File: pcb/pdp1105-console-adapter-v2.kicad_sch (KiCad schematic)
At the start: 15 parts, among them J1 SCL Connector, J2 Aux Terminal Connector, Q1 MMBT3904, U1 Pico, U2 MAX3232

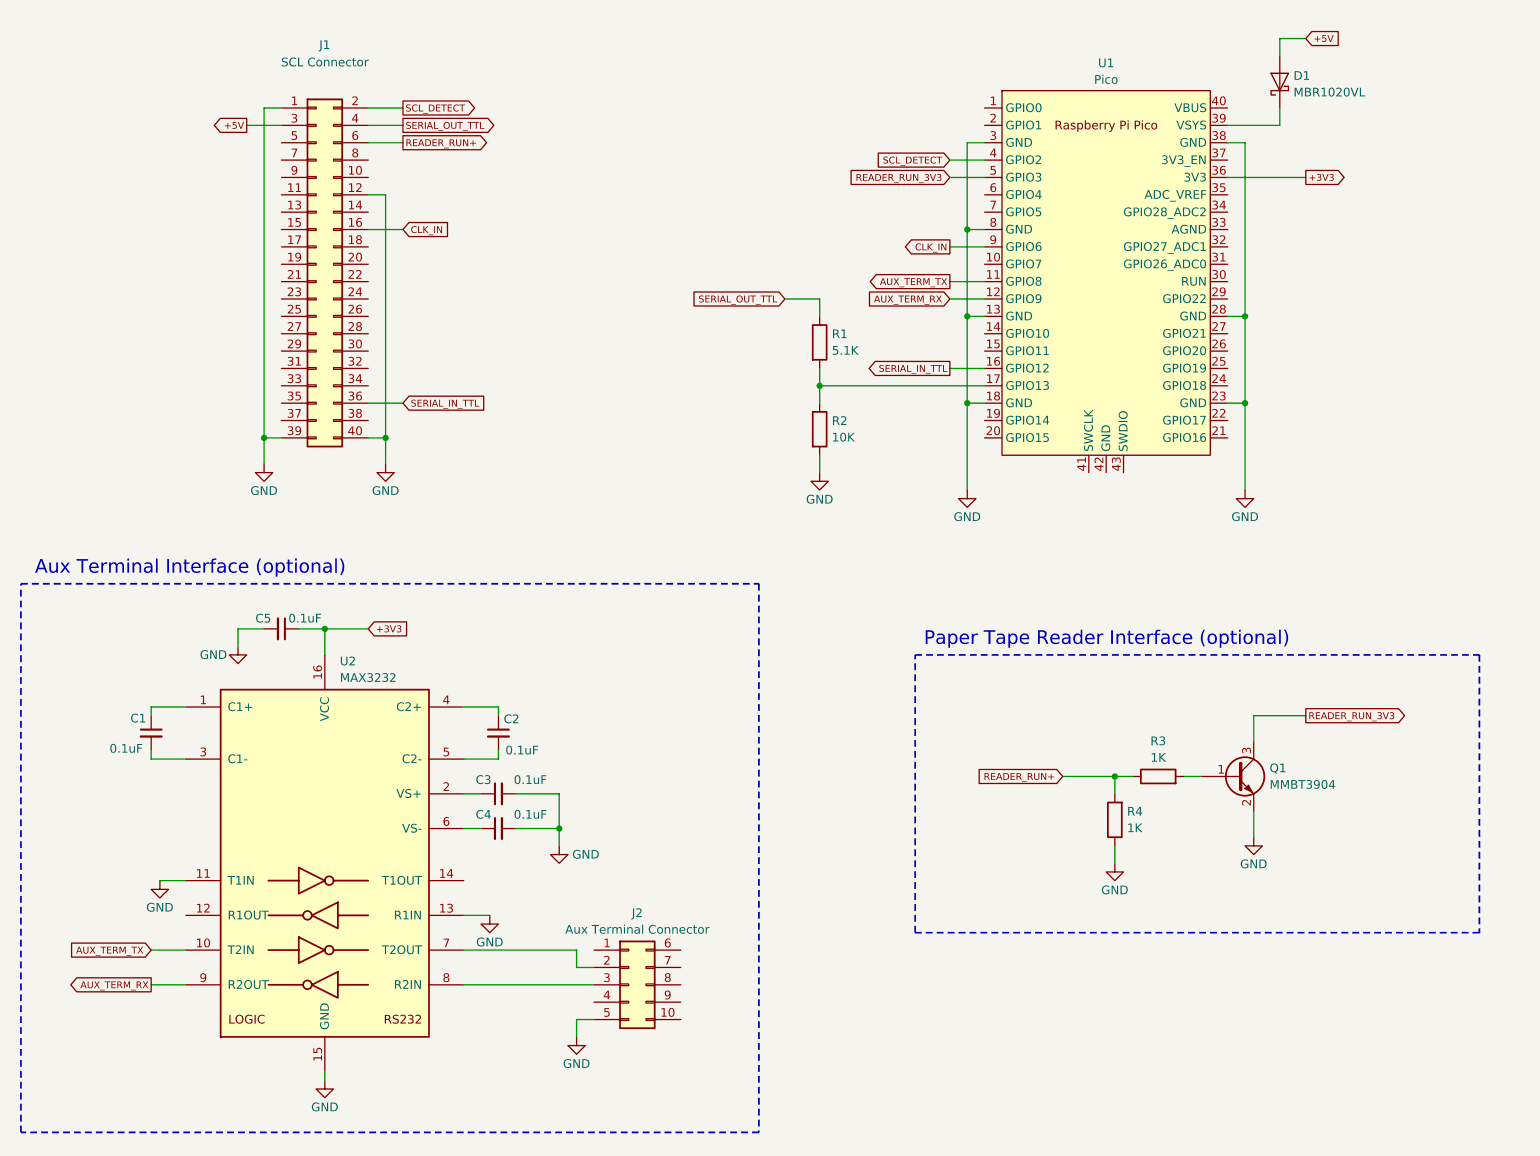
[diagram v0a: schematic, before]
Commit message: ﻿Initial version of Rev 4 schematic
-- Added status LEDs

-- Changed Aux port connector to board-mounted DE9

-- Added mounting hole components
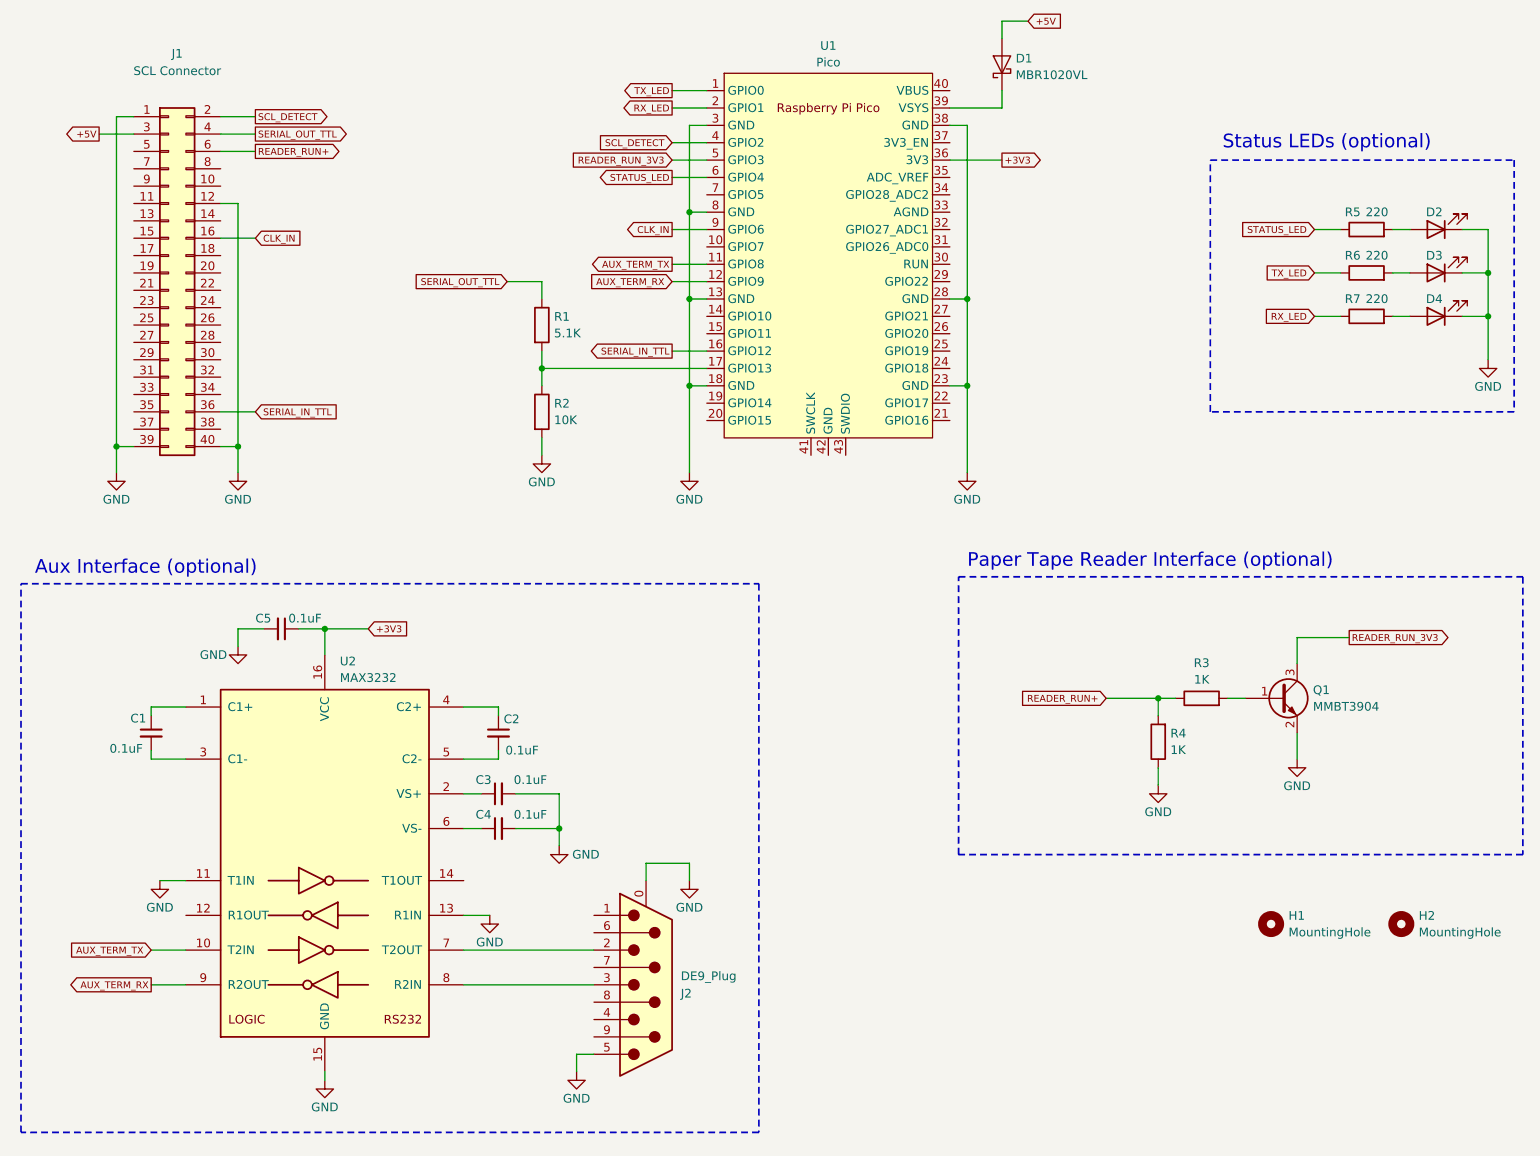
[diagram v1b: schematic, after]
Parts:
- removed J2: Aux Terminal Connector, Connector_PinHeader_2.54mm:PinHeader_2x05_P2.54mm_Vertical, symbol Connector_Generic:Conn_02x05_Top_Bottom
- added D2, D3, D4: LED, LED_THT:LED_D5.0mm, symbol Device:LED
- added H1, H2: MountingHole, MountingHole:MountingHole_2.7mm_M2.5, symbol Mechanical:MountingHole
- added J2: DE9_Plug, Connector_Dsub:DSUB-9_Male_Horizontal_P2.77x2.84mm_EdgePinOffset7.70mm_Housed_MountingHolesOffset9.12mm, symbol Connector:DE9_Plug_MountingHoles
- added R5, R6, R7: 220, Resistor_SMD:R_0805_2012Metric_Pad1.20x1.40mm_HandSolder, symbol Device:R
- J1: footprint Connector_PinHeader_2.54mm:PinHeader_2x20_P2.54mm_Vertical -> Connector_PinSocket_2.54mm:PinSocket_2x20_P2.54mm_Vertical
- U1: footprint MCU_RaspberryPi_and_Boards:RPi_Pico_SMD_TH -> Module:RaspberryPi_Pico_Common_THT
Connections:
- net GND: now also D2.1 (K), D3.1 (K), D4.1 (K), J2.0 (PAD), J2.5
- net TX_LED: now reaches U1.1 (GPIO0)
- net TX_LED: now also R6.1
- net RX_LED: now reaches U1.2 (GPIO1)
- net RX_LED: now also R7.1
- net STATUS_LED: now reaches U1.6 (GPIO4)
- net STATUS_LED: now also R5.1
- net at U2.7 (T2OUT): now also J2.2
- net at U2.8 (R2IN): now also J2.3
- new net: D4.2 (A), R7.2
- new net: D3.2 (A), R6.2
- new net: D2.2 (A), R5.2
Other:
- note added: "Aux Interface (optional)"
- note added: "Status LEDs (optional)"
- note removed: "Aux Terminal Interface (optional)"
- moved on the sheet: D1, J1, Q1, R1, R2, R3, R4, U1

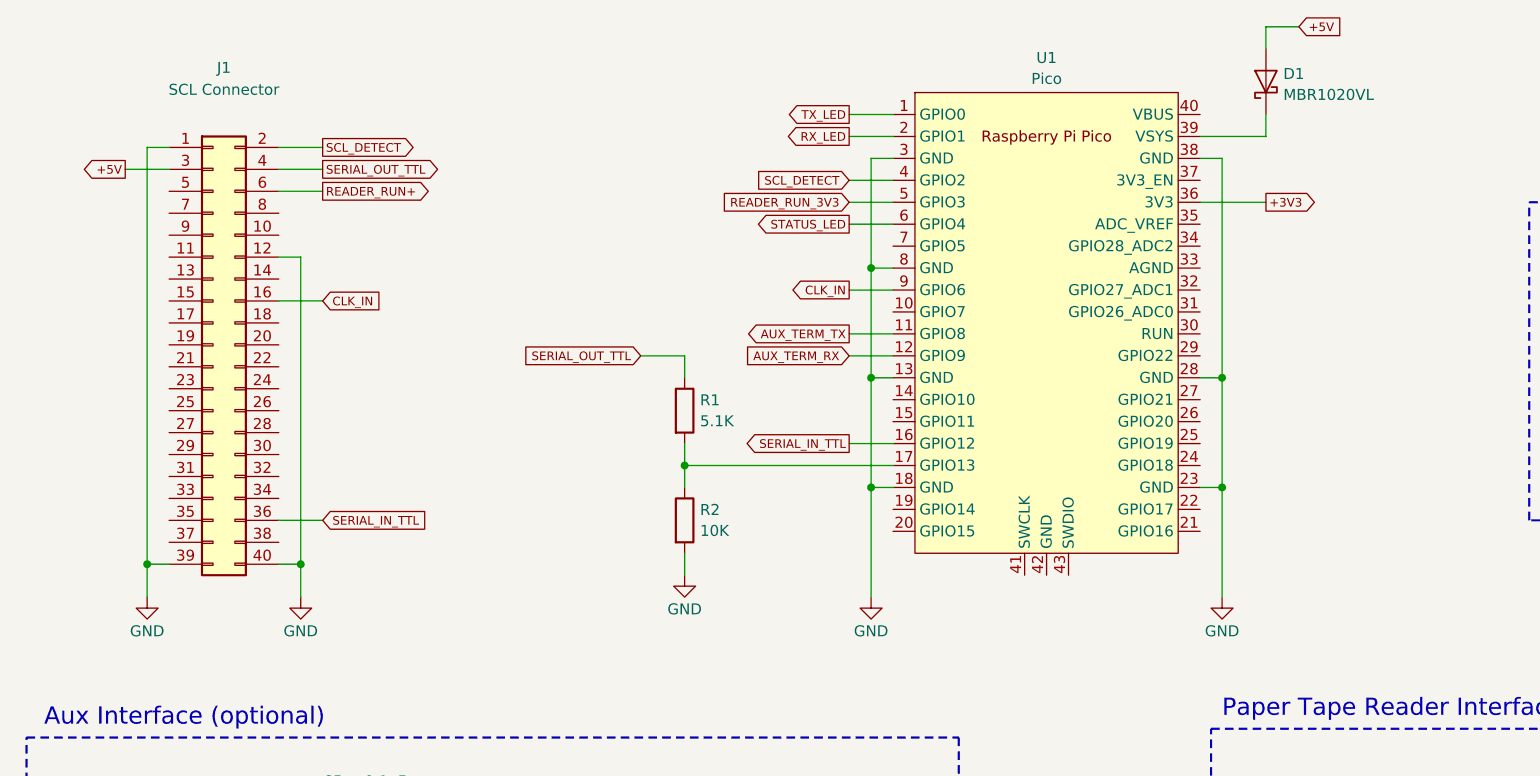
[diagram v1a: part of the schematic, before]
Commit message: ﻿Completed layout and routing for revision 4 PCB
-- NOTE: Pico pin assignments were altered from revision 3 board to simplify routing
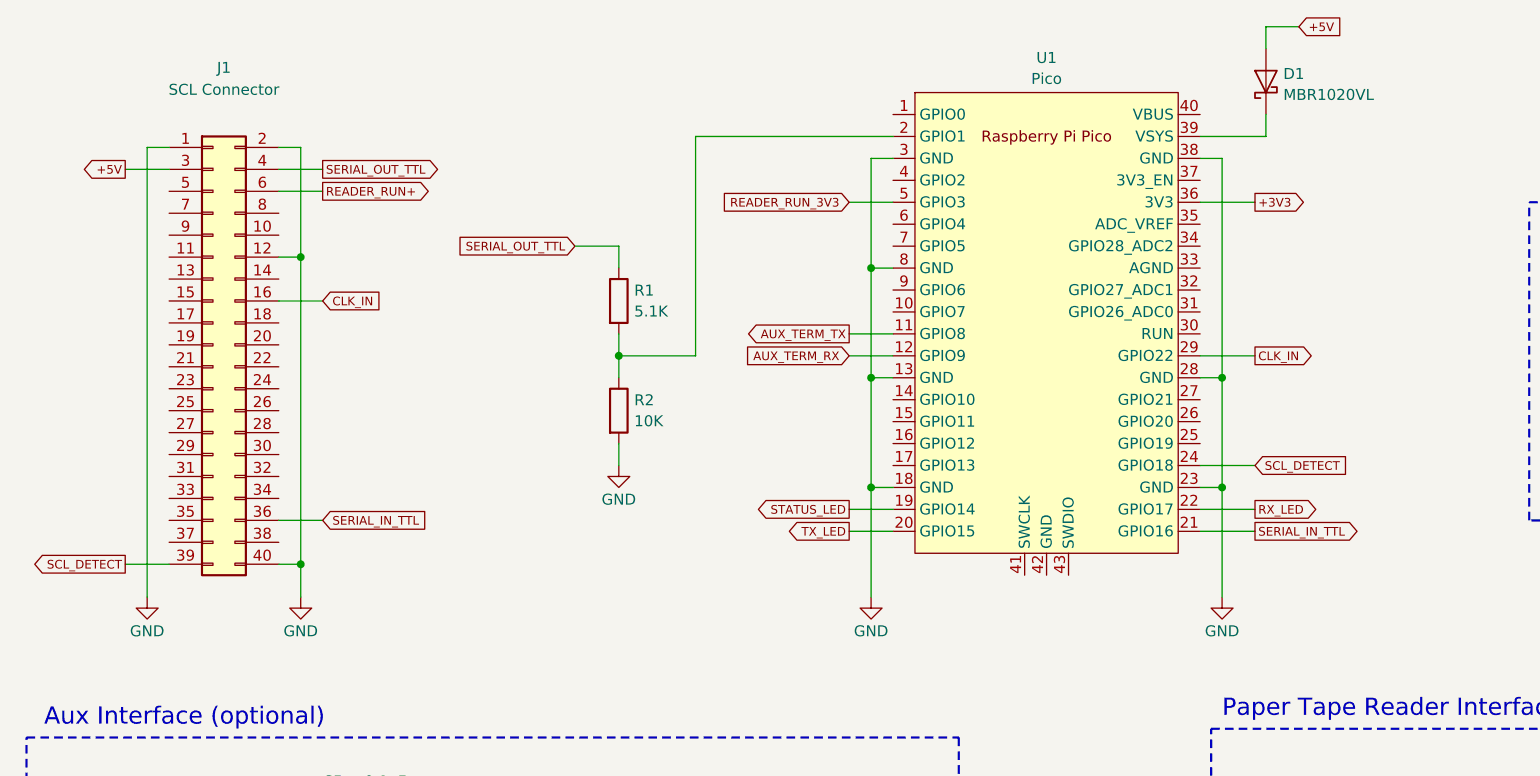
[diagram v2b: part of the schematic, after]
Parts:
- D2, D3, D4, J2: now left out of the parts list
- U1: footprint Module:RaspberryPi_Pico_Common_THT -> pdp1105-console-adapter:RaspberryPi_Pico_Common_THT
- U2: footprint Package_SO:TSSOP-16_4.4x5mm_P0.65mm -> Package_SO:SOIC-16_3.9x9.9mm_P1.27mm; LCSC C13482 -> C9378
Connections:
- net CLK_IN: now also U1.29 (GPIO22); no longer U1.9 (GPIO6)
- net GND: now also J1.2 (GND); no longer J1.39 (GND)
- net RX_LED: now also U1.22 (GPIO17); no longer U1.2 (GPIO1)
- net SCL_DETECT: now also J1.39 (GND), U1.24 (GPIO18); no longer J1.2 (GND), U1.4 (GPIO2)
- net SERIAL_IN_TTL: now also U1.21 (GPIO16); no longer U1.16 (GPIO12)
- net STATUS_LED: now also U1.19 (GPIO14); no longer U1.6 (GPIO4)
- net TX_LED: now also U1.20 (GPIO15); no longer U1.1 (GPIO0)
- net at R1.2, R2.1: now also U1.2 (GPIO1); no longer U1.17 (GPIO13)
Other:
- title: PDP-11/05 Console USB Adapter V2 -> PDP-11/05 Console Adapter V2
- moved on the sheet: R1, R2
